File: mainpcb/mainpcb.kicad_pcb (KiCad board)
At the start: 2 copper layers, 100 x 100 mm, 0 parts

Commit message: Started layout of control board
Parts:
- added C1: 0.1uF, Capacitor_THT:C_Rect_L4.6mm_W2.0mm_P2.50mm_MKS02_FKP02, F.Cu at (-74.4, 122.8)
- added C10: 0.1uF, Capacitor_THT:C_Rect_L4.6mm_W2.0mm_P2.50mm_MKS02_FKP02, F.Cu at (-17.2, 84.5)
- added C11: 0.1uF, Capacitor_THT:C_Rect_L4.6mm_W2.0mm_P2.50mm_MKS02_FKP02, F.Cu at (-53.6, 100.8)
- added C12: 0.1uF, Capacitor_THT:C_Rect_L4.6mm_W2.0mm_P2.50mm_MKS02_FKP02, F.Cu at (-53.6, 104.3)
- added C13: 1uF, Capacitor_THT:C_Rect_L4.6mm_W2.0mm_P2.50mm_MKS02_FKP02, F.Cu at (-53.6, 107.8)
- added C14: 0.1uF, Capacitor_THT:C_Rect_L4.6mm_W2.0mm_P2.50mm_MKS02_FKP02, F.Cu at (-53.6, 111.4)
- added C15: 0.1uF, Capacitor_THT:C_Rect_L4.6mm_W2.0mm_P2.50mm_MKS02_FKP02, F.Cu at (-53.6, 115.0)
- added C16: 0.1uF, Capacitor_THT:C_Rect_L4.6mm_W2.0mm_P2.50mm_MKS02_FKP02, F.Cu at (-53.6, 118.5)
- added C17: 0.1uF, Capacitor_THT:C_Rect_L4.6mm_W2.0mm_P2.50mm_MKS02_FKP02, F.Cu at (-53.6, 122.0)
- added C18: 330uF, Capacitor_THT:C_Radial_D10.0mm_H12.5mm_P5.00mm, F.Cu at (124.5, 101.0)
- added C2: 0.01uF, Capacitor_THT:C_Rect_L4.0mm_W2.5mm_P2.50mm, F.Cu at (117.2, 55.9)
- added C23: 0.1uF, Capacitor_THT:C_Rect_L4.6mm_W2.0mm_P2.50mm_MKS02_FKP02, F.Cu at (-74.4, 126.4)
- added C24: 0.1uF, Capacitor_THT:C_Rect_L4.6mm_W2.0mm_P2.50mm_MKS02_FKP02, F.Cu at (-74.4, 129.9)
- added C3: 82uF, Capacitor_THT:CP_Radial_D8.0mm_P3.50mm, F.Cu at (98.3, 54.0)
- added C4: 0.1uF, Capacitor_THT:C_Rect_L4.0mm_W2.5mm_P2.50mm, F.Cu at (102.7, 54.2)
- added C5: 180uF, Capacitor_THT:CP_Radial_D8.0mm_P3.50mm, F.Cu at (125.2, 57.0)
- added C6: 39uF, Capacitor_THT:CP_Radial_D8.0mm_P3.50mm, F.Cu at (98.2, 97.9)
- added C7: 0.01uF, Capacitor_THT:C_Rect_L4.0mm_W2.5mm_P2.50mm, F.Cu at (116.9, 99.2)
- added C8: 0.1uF, Capacitor_THT:C_Rect_L4.0mm_W2.5mm_P2.50mm, F.Cu at (102.9, 97.9)
- added C9: 0.1uF, Capacitor_THT:C_Rect_L4.6mm_W2.0mm_P2.50mm_MKS02_FKP02, F.Cu at (-17.2, 81.0)
- added D1: LED, LED_THT:LED_D5.0mm_Clear, F.Cu at (-102.0, 124.8)
- added D2: LED, LED_THT:LED_D5.0mm_Clear, F.Cu at (-94.5, 124.8)
- added D3: D_Schottky, Diode_THT:D_DO-27_P15.24mm_Horizontal, F.Cu at (100.2, 59.9)
- added D4: D_Schottky, Diode_THT:D_DO-27_P15.24mm_Horizontal, F.Cu at (100.3, 104.2)
- added J1: Raspberry_Pi_2_3, Connector_PinHeader_2.54mm:PinHeader_2x20_P2.54mm_Vertical, F.Cu at (142.9, 66.0)
- added J10: Conn_02x02_Top_Bottom, Connector_Molex:Molex_Mini-Fit_Jr_5569-04A2_2x02_P4.20mm_Horizontal, F.Cu at (84.8, 134.6)
- added J11: Conn_02x02_Top_Bottom, Connector_Molex:Molex_Mini-Fit_Jr_5569-04A2_2x02_P4.20mm_Horizontal, F.Cu at (214.9, 129.9)
- added J13: Screw_Terminal_01x09, TerminalBlock_Phoenix:TerminalBlock_Phoenix_PT-1,5-9-5.0-H_1x09_P5.00mm_Horizontal, F.Cu at (219.7, 105.0)
- added J15: Screw_Terminal_01x02, TerminalBlock_Phoenix:TerminalBlock_Phoenix_PT-1,5-2-5.0-H_1x02_P5.00mm_Horizontal, F.Cu at (219.7, 58.6)
- added J2: 8P8C_Shielded, Connector_RJ:RJ45_Amphenol_54602-x08_Horizontal, F.Cu at (83.8, 112.7)
- added J3: 8P8C_Shielded, Connector_RJ:RJ45_Amphenol_54602-x08_Horizontal, F.Cu at (215.9, 121.3)
- added J4: Screw_Terminal_01x09, TerminalBlock_Phoenix:TerminalBlock_Phoenix_PT-1,5-9-5.0-H_1x09_P5.00mm_Horizontal, F.Cu at (80.0, 65.0)
- added J5: 8PCV-06-006, bh_footprint_library:Terminal_Block_8PCV-06-006, F.Cu at (-116.9, 40.6)
- added J6: Conn_01x08, Connector_PinHeader_2.54mm:PinHeader_1x08_P2.54mm_Vertical, F.Cu at (-16.7, 40.1)
- added J7: Conn_01x08, Connector_PinHeader_2.54mm:PinHeader_1x08_P2.54mm_Vertical, F.Cu at (-12.0, 40.1)
- added J8: Conn_01x03, Connector_PinHeader_2.54mm:PinHeader_1x03_P2.54mm_Vertical, F.Cu at (-16.7, 62.5)
- added J9: Screw_Terminal_01x02, TerminalBlock_Phoenix:TerminalBlock_Phoenix_PT-1,5-2-5.0-H_1x02_P5.00mm_Horizontal, F.Cu at (80.0, 53.6)
- added L1: 33uH, Inductor_THT:L_Toroid_Vertical_L31.8mm_W15.9mm_P13.50mm_Bourns_5700, F.Cu at (120.0, 62.2)
- added L2: 15uH, Inductor_THT:L_Toroid_Vertical_L31.8mm_W15.9mm_P13.50mm_Bourns_5700, F.Cu at (120.0, 106.1)
- added R1: 330R, Resistor_THT:R_Axial_DIN0207_L6.3mm_D2.5mm_P10.16mm_Horizontal, F.Cu at (-88.0, 123.1)
- added R10: 10kR, Resistor_THT:R_Axial_DIN0207_L6.3mm_D2.5mm_P10.16mm_Horizontal, F.Cu at (-30.7, 68.2)
- added R11: 120R, Resistor_THT:R_Axial_DIN0207_L6.3mm_D2.5mm_P10.16mm_Horizontal, F.Cu at (-30.7, 72.2)
- added R12: 120R, Resistor_THT:R_Axial_DIN0207_L6.3mm_D2.5mm_P10.16mm_Horizontal, F.Cu at (-30.7, 76.3)
- added R13: 600R, Resistor_THT:R_Axial_DIN0207_L6.3mm_D2.5mm_P10.16mm_Horizontal, F.Cu at (-30.7, 80.3)
- added R14: 600R, Resistor_THT:R_Axial_DIN0207_L6.3mm_D2.5mm_P10.16mm_Horizontal, F.Cu at (-30.7, 84.4)
- added R15: 120R, Resistor_THT:R_Axial_DIN0207_L6.3mm_D2.5mm_P10.16mm_Horizontal, F.Cu at (-30.7, 88.4)
- added R16: 120R, Resistor_THT:R_Axial_DIN0207_L6.3mm_D2.5mm_P10.16mm_Horizontal, F.Cu at (-30.7, 92.5)
- added R17: 904R, Resistor_THT:R_Axial_DIN0207_L6.3mm_D2.5mm_P10.16mm_Horizontal, F.Cu at (-47.8, 101.0)
- added R18: 3k, Resistor_THT:R_Axial_DIN0207_L6.3mm_D2.5mm_P10.16mm_Horizontal, F.Cu at (-47.8, 105.0)
- added R19: 1k, Resistor_THT:R_Axial_DIN0207_L6.3mm_D2.5mm_P10.16mm_Horizontal, F.Cu at (-47.8, 109.1)
- added R2: 330R, Resistor_THT:R_Axial_DIN0207_L6.3mm_D2.5mm_P10.16mm_Horizontal, F.Cu at (-88.0, 127.2)
- added R20: 1k, Resistor_THT:R_Axial_DIN0207_L6.3mm_D2.5mm_P10.16mm_Horizontal, F.Cu at (-47.8, 113.2)
- added R21: 4k, Resistor_THT:R_Axial_DIN0207_L6.3mm_D2.5mm_P10.16mm_Horizontal, F.Cu at (-47.8, 117.2)
- added R3: 120R, Resistor_THT:R_Axial_DIN0207_L6.3mm_D2.5mm_P10.16mm_Horizontal, F.Cu at (-30.7, 39.8)
- added R4: 120R, Resistor_THT:R_Axial_DIN0207_L6.3mm_D2.5mm_P10.16mm_Horizontal, F.Cu at (-30.7, 43.9)
- added R5: 600R, Resistor_THT:R_Axial_DIN0207_L6.3mm_D2.5mm_P10.16mm_Horizontal, F.Cu at (-30.7, 47.9)
- added R6: 600R, Resistor_THT:R_Axial_DIN0207_L6.3mm_D2.5mm_P10.16mm_Horizontal, F.Cu at (-30.7, 52.0)
- added R7: 120R, Resistor_THT:R_Axial_DIN0207_L6.3mm_D2.5mm_P10.16mm_Horizontal, F.Cu at (-30.7, 56.0)
- added R8: 120R, Resistor_THT:R_Axial_DIN0207_L6.3mm_D2.5mm_P10.16mm_Horizontal, F.Cu at (-30.7, 60.1)
- added R9: 10kR, Resistor_THT:R_Axial_DIN0207_L6.3mm_D2.5mm_P10.16mm_Horizontal, F.Cu at (-30.7, 64.1)
- added REF**: MountingHole_2.7mm_M2.5, MountingHole:MountingHole_2.7mm_M2.5, F.Cu at (155.9, 59.9)
- added REF**: MountingHole_2.7mm_M2.5, MountingHole:MountingHole_2.7mm_M2.5, F.Cu at (204.9, 59.9)
- added REF**: MountingHole_2.7mm_M2.5, MountingHole:MountingHole_2.7mm_M2.5, F.Cu at (155.9, 117.9)
- added REF**: MountingHole_2.7mm_M2.5, MountingHole:MountingHole_2.7mm_M2.5, F.Cu at (204.9, 117.9)
- added U1: TCA9517ADGK, Package_SO:VSSOP-8_3x3mm_P0.65mm, F.Cu at (-100.8, 131.0)
- added U10: LM4040LP-4.1, Package_TO_SOT_THT:TO-92_Inline, F.Cu at (-38.2, 122.5)
- added U11: TMCS1108A3BQDR, Package_SO:SOIC-8-N7_3.9x4.9mm_P1.27mm, F.Cu at (200.9, 128.5)
- added U12: TMCS1108A3BQDR, Package_SO:SOIC-8-N7_3.9x4.9mm_P1.27mm, F.Cu at (200.9, 135.5)
- added U2: TXB0108PW, Package_SO:TSSOP-20_4.4x6.5mm_P0.65mm, F.Cu at (47.0, 75.1)
- added U3: LM2678T-12, Package_TO_SOT_THT:TO-220-7_P2.54x3.7mm_StaggerOdd_Lead3.8mm_Vertical, F.Cu at (106.0, 58.0)
- added U4: LM2678T-5, Package_TO_SOT_THT:TO-220-7_P2.54x3.7mm_StaggerOdd_Lead3.8mm_Vertical, F.Cu at (106.1, 101.6)
- added U5: PCA9615DP, Package_SO:TSSOP-10_3x3mm_P0.5mm, F.Cu at (-15.5, 72.2)
- added U6: PCA9615DP, Package_SO:TSSOP-10_3x3mm_P0.5mm, F.Cu at (-15.5, 76.9)
- added U7: TMCS1108A3BQDR, Package_SO:SOIC-8-N7_3.9x4.9mm_P1.27mm, F.Cu at (99.0, 135.7)
- added U8: TMCS1108A3BQDR, Package_SO:SOIC-8-N7_3.9x4.9mm_P1.27mm, F.Cu at (99.0, 128.7)
- added U9: ADS7828, Package_SO:TSSOP-16_4.4x5mm_P0.65mm, F.Cu at (-44.6, 122.5)
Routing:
- net Net-(D3-K): track 0.00 -> 37.1 mm
- net Net-(D4-K): track 0.00 -> 37.0 mm
- net +12V: track 0.00 -> 34.7 mm
- net +5V: track 0.00 -> 20.5 mm
- net +24V: track 0.00 -> 18.3 mm
- net Net-(U3-CB): track 0.00 -> 9.51 mm
- net Net-(U4-CB): track 0.00 -> 9.24 mm
- added copper zone on B.Cu, net GND
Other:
- board size 100 x 100 mm -> 150 x 120 mm
- board text added: "HEAT SINK KEEPOUT ZONE"

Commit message: Continued control board layout
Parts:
- moved J5 340.4 mm to (210.3, 134.7), turned to 180 degrees
- moved C16 284.5 mm to (229.2, 148.6), turned to 180 degrees
- moved C17 280.3 mm to (226.6, 125.5)
- moved R4 272.7 mm to (233.0, 113.0), turned to 180 degrees
- moved R8 267.8 mm to (233.0, 106.7), turned to 180 degrees
- moved R12 266.8 mm to (233.0, 116.2), turned to 180 degrees
- moved R16 265.5 mm to (233.0, 122.5), turned to 180 degrees
- moved R6 260.1 mm to (222.9, 109.8)
- moved R14 256.0 mm to (222.9, 119.4)
- moved J7 247.5 mm to (228.1, 100.0), turned to -90 degrees
- moved U6 234.6 mm to (216.1, 114.3)
- moved C10 234.5 mm to (215.9, 109.8), turned to 90 degrees
- moved C12 184.3 mm to (127.7, 137.4)
- moved C13 184.3 mm to (127.7, 141.0)
- moved U9 166.9 mm to (121.6, 138.7), turned to 90 degrees
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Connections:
- J13 pad 1: GND -> Net-(J13-Pin_1)
- J13 pad 2: unconnected-(J13-Pin_2-Pad2) -> GND
- J13 pad 9: Net-(J13-Pin_9) -> GND
- J2 pad 3: DSDA1+ -> DSCL1-
- J2 pad 4: DSDA1- -> DSCL1+
- J2 pad 5: DSCL1+ -> DSDA1+
- J2 pad 6: DSCL1- -> DSDA1-
- J3 pad 3: DSDA2+ -> DSCL2-
- J3 pad 4: DSDA2- -> DSCL2+
- J3 pad 5: DSCL2+ -> DSDA2+
- J3 pad 6: DSCL2- -> DSDA2-
- J4 pad 1: GND -> Net-(J4-Pin_1)
- J4 pad 2: unconnected-(J4-Pin_2-Pad2) -> GND
- J4 pad 9: Net-(J4-Pin_9) -> GND
- U11 pad 3: Net-(J11-Pin_3) -> Net-(J11-Pin_4)
- U11 pad 4: Net-(J11-Pin_3) -> Net-(J11-Pin_4)
- U12 pad 3: Net-(J11-Pin_4) -> Net-(J11-Pin_3)
- U12 pad 4: Net-(J11-Pin_4) -> Net-(J11-Pin_3)
- U2 pad 12: Net-(J13-Pin_3) -> Net-(J13-Pin_7)
- U2 pad 14: Net-(J13-Pin_7) -> Net-(J13-Pin_3)
- U2 pad 15: Net-(J13-Pin_9) -> Net-(J13-Pin_1)
- U2 pad 16: Net-(J4-Pin_3) -> Net-(J4-Pin_7)
- U2 pad 18: Net-(J4-Pin_7) -> Net-(J4-Pin_3)
- U2 pad 20: Net-(J4-Pin_9) -> Net-(J4-Pin_1)
- U7 pad 3: Net-(J10-Pin_3) -> Net-(J10-Pin_4)
- U7 pad 4: Net-(J10-Pin_3) -> Net-(J10-Pin_4)
- U8 pad 3: Net-(J10-Pin_4) -> Net-(J10-Pin_3)
- U8 pad 4: Net-(J10-Pin_4) -> Net-(J10-Pin_3)
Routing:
- net Net-(J4-Pin_7): track 0.00 -> 37.4 mm, vias 0 -> 1
- net DSCL1-: track 0.00 -> 33.5 mm
- net DSCL2-: track 0.00 -> 31.3 mm
- net Net-(J4-Pin_5): track 0.00 -> 31.1 mm, vias 0 -> 1
- net DSDA2-: track 0.00 -> 30.6 mm
- net DSDA2+: track 0.00 -> 29.1 mm
- net DSDA1-: track 0.00 -> 29.0 mm
- net Net-(J4-Pin_1): track 0.00 -> 28.4 mm, vias 0 -> 1
- net DSDA1+: track 0.00 -> 28.2 mm
- net DSCL1+: track 0.00 -> 26.7 mm
- net Net-(J4-Pin_3): track 0.00 -> 25.5 mm, vias 0 -> 1
- net DSCL2+: track 0.00 -> 25.4 mm
- net Net-(J13-Pin_1): track 0.00 -> 21.1 mm
- net Net-(J13-Pin_3): track 0.00 -> 21.1 mm
- net Net-(J13-Pin_5): track 0.00 -> 21.1 mm
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- added copper zone on F.Cu, net +12V
- added copper zone on F.Cu, net +24V
- added copper zone on B.Cu, net +5V
- added copper zone on F.Cu, net +5V
- added copper zone on F.Cu, net Net-(J10-Pin_3)
- added copper zone on F.Cu, net Net-(J10-Pin_4)
- added copper zone on F.Cu, net Net-(J11-Pin_3)
- added copper zone on F.Cu, net Net-(J11-Pin_4)
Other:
- board size 150 x 120 mm -> 200 x 120 mm
- board text added: "24V"
- board text added: "ALARM+"
- board text added: "ALARM-"
- board text added: "COM"
- board text added: "DIR+"
- board text added: "DIR-"
- board text added: "ENA+"
- board text added: "ENA-"
- board text added: "GND"
- board text added: "PUL+"
- board text added: "PUL-"

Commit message: Started signal track layout of control PCB
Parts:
- moved U1 191.9 mm to (90.4, 114.9), turned to -90 degrees
- moved C24 160.7 mm to (85.1, 110.5)
- moved C16 69.7 mm to (226.7, 78.9), turned to 0 degrees
- moved J6 64.2 mm to (14.6, 69.8)
- moved J8 63.3 mm to (24.1, 62.9)
- moved R10 63.3 mm to (16.5, 58.4)
- moved R9 63.3 mm to (16.5, 54.4)
- moved J10 60.3 mm to (60.7, 73.7)
- moved J2 60.3 mm to (59.7, 51.8)
- moved R11 60.3 mm to (67.9, 53.4)
- moved R3 60.3 mm to (67.9, 56.6)
- moved R5 60.3 mm to (78.1, 59.7)
- moved U5 60.3 mm to (85.1, 55.2)
- moved C9 60.3 mm to (85.1, 51.5)
- moved R13 60.3 mm to (78.1, 50.2)
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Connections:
- J1 pad 11: unconnected-(J1-GPIO17-Pad11) -> LED1
- J1 pad 13: unconnected-(J1-GPIO27-Pad13) -> LED2
- J1 pad 15: unconnected-(J1-GPIO22-Pad15) -> PUL1+
- J1 pad 16: unconnected-(J1-GPIO23-Pad16) -> DIR1+
- J1 pad 18: unconnected-(J1-GPIO24-Pad18) -> ENA1+
- J1 pad 22: unconnected-(J1-GPIO25-Pad22) -> ALARM1+
- J1 pad 29: unconnected-(J1-GCLK1/GPIO5-Pad29) -> PUL2+
- J1 pad 31: unconnected-(J1-GCLK2/GPIO6-Pad31) -> DIR2+
- J1 pad 32: unconnected-(J1-PWM0/GPIO12-Pad32) -> ENA2+
- J1 pad 33: unconnected-(J1-PWM1/GPIO13-Pad33) -> ALARM2+
- J1 pad 36: unconnected-(J1-GPIO16-Pad36) -> LIMIT_SW_LL
- J1 pad 37: unconnected-(J1-GPIO26-Pad37) -> LIMIT_SW_RR
- J1 pad 38: unconnected-(J1-GPIO20/MOSI1-Pad38) -> LIMIT_SW_LR
- J1 pad 40: unconnected-(J1-GPIO21/SCLK1-Pad40) -> LIMIT_SW_RL
- R18 pad 2: Net-(U9-CH4) -> Net-(U9-CH5)
- R19 pad 2: Net-(U9-CH5) -> Net-(U9-CH4)
- R20 pad 1: Net-(U9-CH4) -> Net-(U9-CH5)
- R21 pad 1: Net-(U9-CH5) -> Net-(U9-CH4)
- U9 pad 7: +3.3V -> unconnected-(U9-CH6-Pad7)
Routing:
- net +12V: track 34.7 -> 352.5 mm, vias 0 -> 52
- net +5V: track 20.5 -> 333.4 mm, vias 52 -> 0
- net +24V: track 18.3 -> 274.4 mm
- net ENA2+: track 0.00 -> 41.6 mm
- net ALARM2+: track 0.00 -> 39.2 mm
- net DIR2+: track 0.00 -> 37.2 mm
- net PUL2+: track 0.00 -> 35.3 mm
- net ALARM1+: track 0.00 -> 28.3 mm
- net ENA1+: track 0.00 -> 27.2 mm
- net DIR1+: track 0.00 -> 25.3 mm
- net PUL1+: track 0.00 -> 22.2 mm
- net +3.3V: track 0.00 -> 18.5 mm, vias 0 -> 1
- net Net-(U9-CH5): track 0.00 -> 18.5 mm
- net Net-(J11-Pin_4): track 0.00 -> 17.7 mm
- net Net-(U9-CH4): track 0.00 -> 15.8 mm
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- added copper zone on B.Cu, net +12V

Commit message: Completed control board layout
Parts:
- added H1: MountingHole, MountingHole:MountingHole_4.3mm_M4, F.Cu at (56.0, 37.0)
- added H2: MountingHole, MountingHole:MountingHole_4.3mm_M4, F.Cu at (56.0, 147.0)
- added H3: MountingHole, MountingHole:MountingHole_4.3mm_M4, F.Cu at (246.0, 37.0)
- added H4: MountingHole, MountingHole:MountingHole_4.3mm_M4, F.Cu at (246.0, 147.0)
- added R22: 10kR, Resistor_THT:R_Axial_DIN0207_L6.3mm_D2.5mm_P10.16mm_Horizontal, F.Cu at (102.2, 116.8)
- added R23: 10kR, Resistor_THT:R_Axial_DIN0207_L6.3mm_D2.5mm_P10.16mm_Horizontal, F.Cu at (102.2, 113.7)
- U11, U12, U7, U8: footprint Package_SO:SOIC-8-N7_3.9x4.9mm_P1.27mm -> Package_SO:SOIC-8_3.9x4.9mm_P1.27mm
- moved D1 165.8 mm to (63.0, 141.0)
- moved D2 165.8 mm to (70.5, 141.0)
- moved C1 159.6 mm to (85.1, 116.2), turned to -90 degrees
- moved R1 152.7 mm to (63.0, 146.1)
- moved R2 152.5 mm to (63.0, 149.2)
- moved C23 149.6 mm to (74.3, 109.9), turned to -90 degrees
- moved R9 133.2 mm to (138.4, 108.0), turned to -90 degrees
- moved R10 132.9 mm to (135.3, 118.1), turned to 90 degrees
- moved J8 132.3 mm to (138.4, 129.5)
- moved J6 71.7 mm to (80.6, 41.9), turned to -90 degrees
- moved C15 71.2 mm to (75.5, 89.5)
- moved C14 70.6 mm to (75.5, 77.5)
- moved C10 58.5 mm to (213.6, 51.4)
- moved J7 58.0 mm to (220.3, 41.9), turned to 90 degrees
- moved R17 19.0 mm to (118.1, 133.3), turned to -90 degrees
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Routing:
- net +5V: track 333.4 -> 660.2 mm, vias 0 -> 10
- net SDA: track 0.00 -> 310.4 mm, vias 0 -> 14
- net SCL: track 0.00 -> 309.8 mm, vias 0 -> 16
- net Net-(J13-Pin_7): track 7.97 -> 198.5 mm, vias 0 -> 6
- net LIMIT_SW_RL: track 0.00 -> 189.1 mm, vias 0 -> 7
- net Net-(J13-Pin_5): track 7.05 -> 189.2 mm, vias 0 -> 6
- net LIMIT_SW_RR: track 0.00 -> 182.1 mm, vias 0 -> 7
- net Net-(J13-Pin_1): track 5.62 -> 186.6 mm, vias 0 -> 6
- net Net-(J13-Pin_3): track 6.14 -> 185.3 mm, vias 0 -> 6
- net Net-(U12-VOUT): track 0.00 -> 160.0 mm, vias 0 -> 6
- net Net-(U11-VOUT): track 0.00 -> 147.3 mm, vias 0 -> 6
- net Net-(U7-VOUT): track 0.00 -> 134.3 mm, vias 0 -> 6
- net Net-(U8-VOUT): track 0.00 -> 120.2 mm, vias 0 -> 6
- net LED2: track 0.00 -> 73.5 mm, vias 0 -> 3
- net LED1: track 0.00 -> 70.0 mm, vias 0 -> 3
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- removed copper zone on B.Cu, net +5V
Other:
- board text added: "BOT-HOVEN"
- board text added: "CONTROL BOARD VERSION 1"
- board text added: "DSCL+"
- board text added: "DSCL-"
- board text added: "DSDA+"
- board text added: "DSDA-"
- board text added: "TRISTAN DOBROWNEY EVAN EVANIUK CORBEN KOLASKI JASCHA PETERSEN ALESSANDRO POTENZA ANTONY ZAKY DESIGNED BY J. PETERSEN"

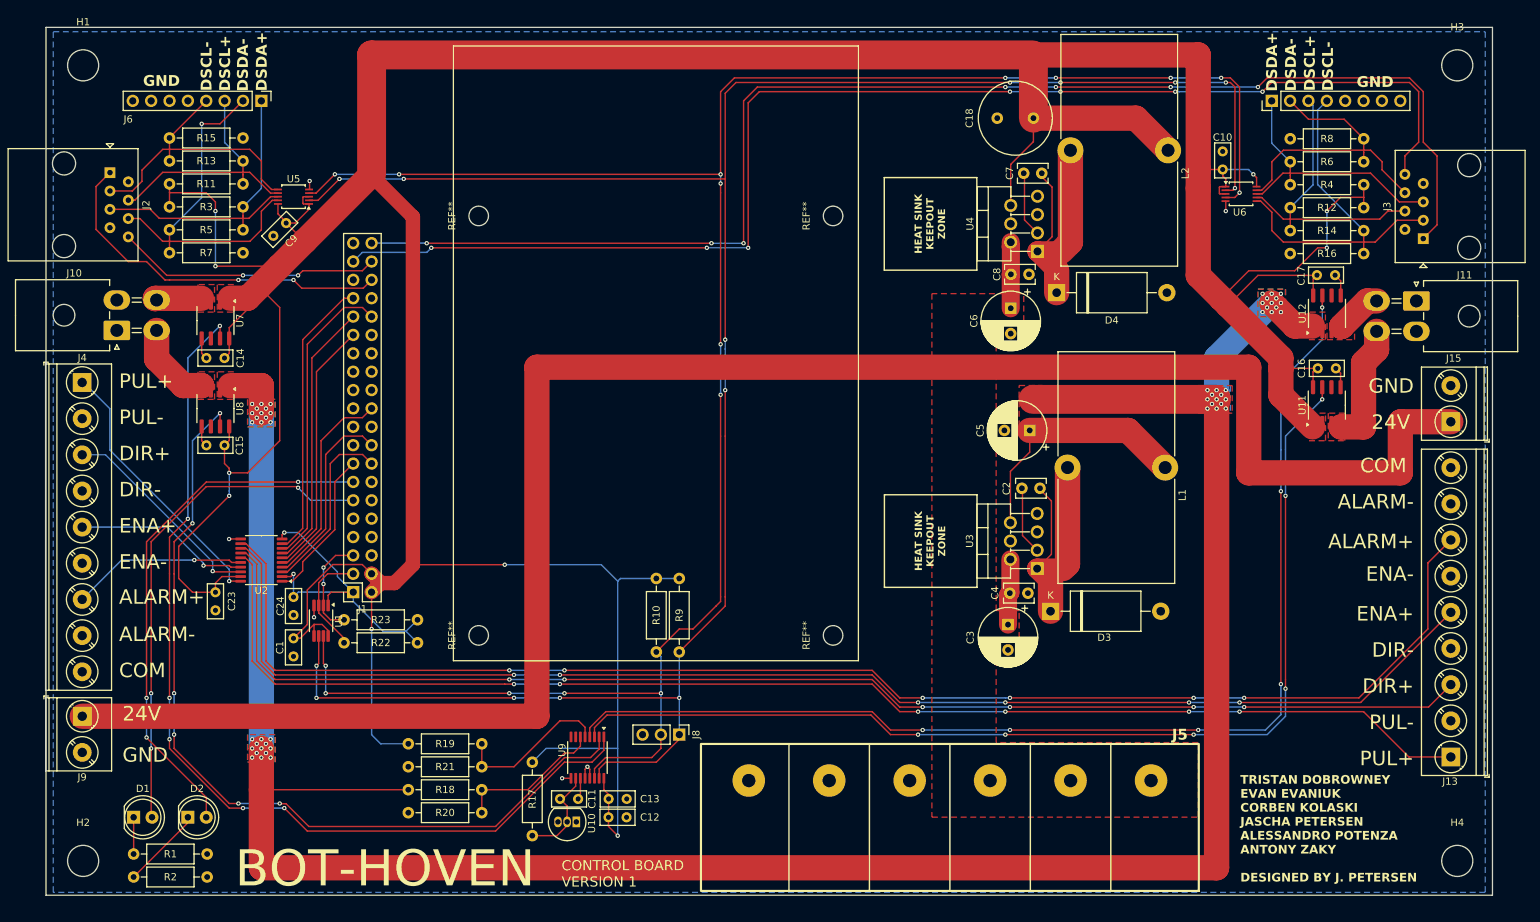
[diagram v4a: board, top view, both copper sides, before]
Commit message: As-Produced commit
This commit contains the PCBs as they were sent to the manufacturer
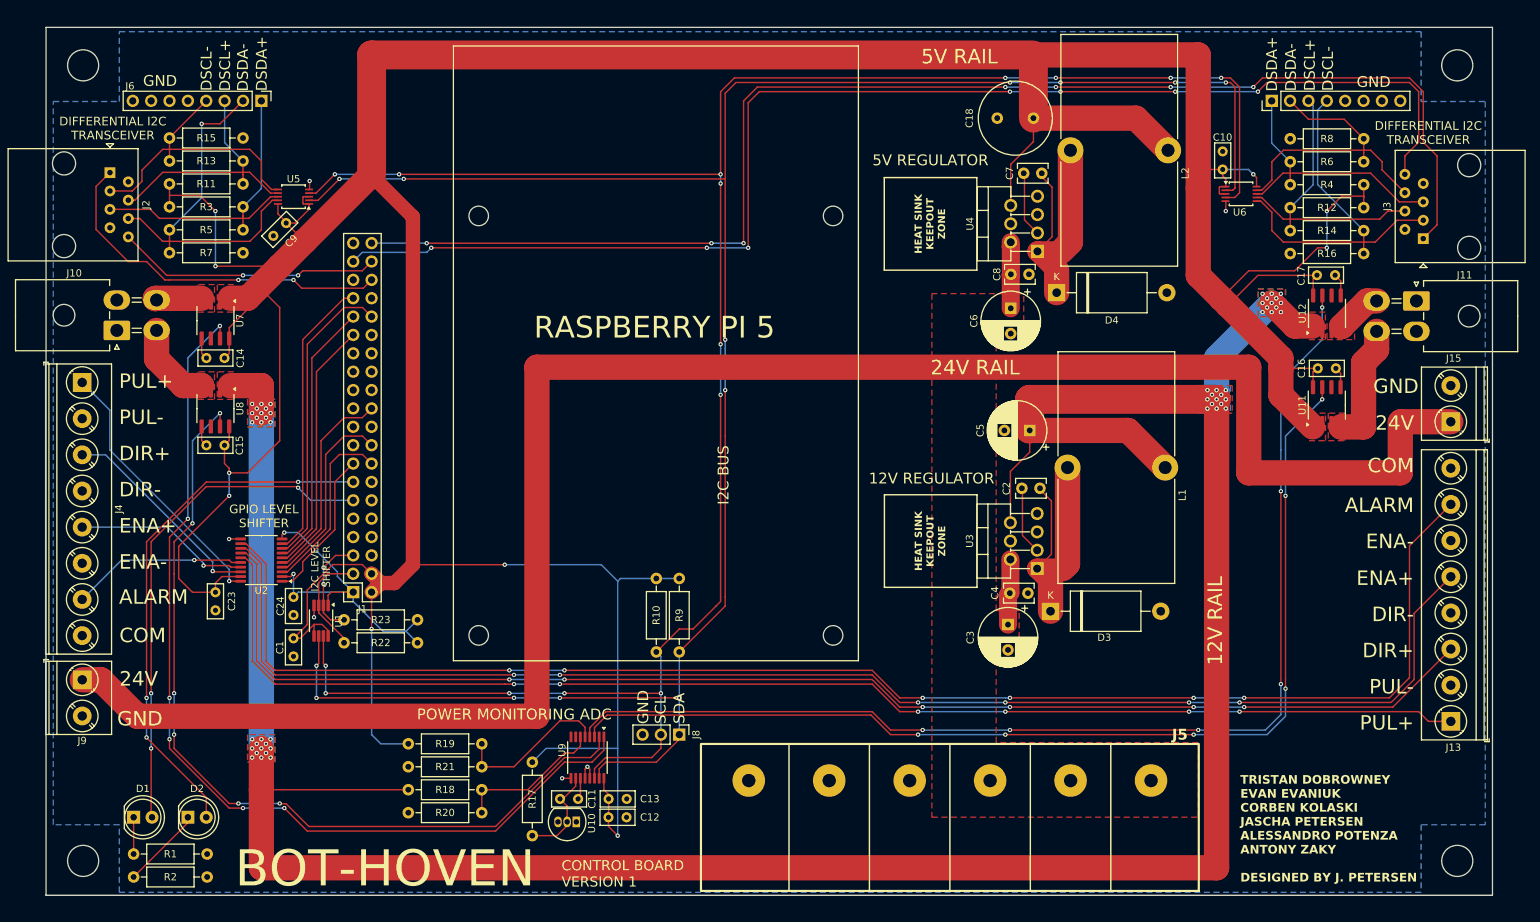
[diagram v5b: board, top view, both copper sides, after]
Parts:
- J13, J4: value Screw_Terminal_01x09 -> Screw_Terminal_01x08; footprint TerminalBlock_Phoenix:TerminalBlock_Phoenix_PT-1,5-9-5.0-H_1x09_P5.00mm_Horizontal -> TerminalBlock_Phoenix:TerminalBlock_Phoenix_PT-1,5-8-5.0-H_1x08_P5.00mm_Horizontal
- moved J9 5.04 mm to (55.9, 122.0)
- moved J13 4.92 mm to (245.1, 127.7)
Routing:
- net Net-(J13-Pin_5): track 189.2 -> 196.6 mm
- net Net-(J13-Pin_7): track 198.5 -> 205.8 mm
- net +12V: track 373.0 -> 377.6 mm
- net +24V: track 277.4 -> 279.5 mm
- net Net-(J13-Pin_1): track 186.6 -> 184.5 mm
- net Net-(J13-Pin_3): track 185.3 -> 187.4 mm
- net +5V: track 660.2 -> 659.5 mm
- net SDA: vias 14 -> 13
- net SCL: vias 16 -> 15
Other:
- board text added: "12V RAIL"
- board text added: "12V REGULATOR"
- board text added: "24V RAIL"
- board text added: "5V RAIL"
- board text added: "5V REGULATOR"
- board text added: "ALARM"
- board text added: "DIFFERENTIAL I2C TRANSCEIVER"
- board text added: "GPIO LEVEL SHIFTER"
- board text added: "I2C BUS"
- board text added: "I2C LEVEL SHIFTER"
- board text added: "POWER MONITORING ADC"
- board text added: "RASPBERRY PI 5"
- board text added: "SCL"
- board text added: "SDA"
- board text removed: "ALARM+"
- board text removed: "ALARM-"
